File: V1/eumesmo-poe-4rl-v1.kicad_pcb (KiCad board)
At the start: 4 copper layers, 99.5 x 45 mm, 125 parts, among them J1 USB_C_Receptacle_USB2.0, J2 RJ45 JACK, J3 250-202, J4 250-202, J5 250-202, J6 250-202, K1 G5NB-1A-E-DC5, K2 G5NB-1A-E-DC5, K3 G5NB-1A-E-DC5, K4 G5NB-1A-E-DC5, Q1 UMH3N, Q2 WPM2015-3/TR, Q3 LMUN2211LT1G, Q4 MMBT2222A, Q5 MMBT2222A, Q6 MMBT2222A, Q7 MMBT2222A, SW1 RESET, U1 CH340K, U2 ESP32-WROOM-32UE-N16, U3 LAN8710A, U4 TPS2376DDAR-H, U5 TX4138, U6 SY8089A1AAC

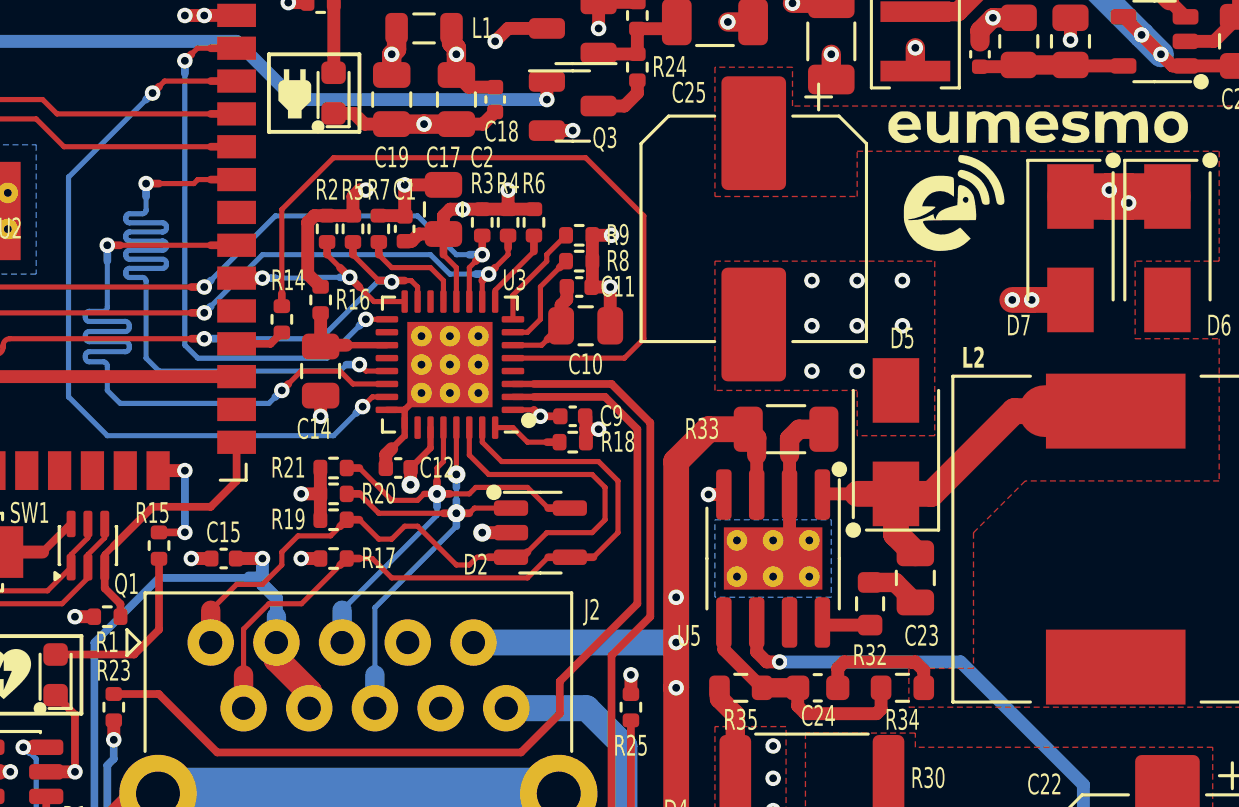
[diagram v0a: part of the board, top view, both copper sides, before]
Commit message: Tweaks to the ethernet signals tracks.
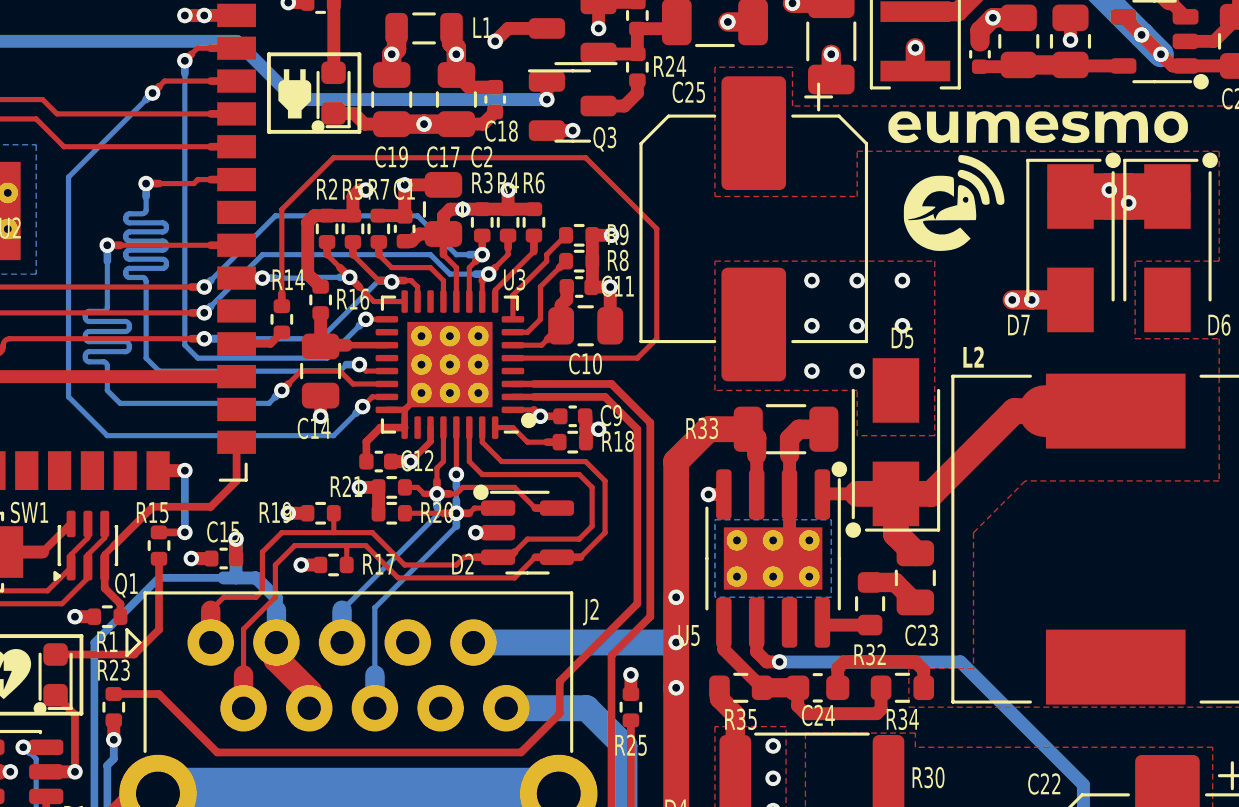
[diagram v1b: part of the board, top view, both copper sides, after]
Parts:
- moved R20 2.37 mm to (140.5, 93.2)
- moved R21 2.37 mm to (140.5, 92.2)
- moved C12 0.79 mm to (140.0, 91.2)
- moved R19 0.56 mm to (137.8, 93.2)
- moved D2 0.50 mm to (145.8, 94.0)
- moved R17 0.25 mm to (138.2, 95.2)
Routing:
- net /ETHTXD-: track 19.6 -> 16.4 mm
- net /ETHTXD+: track 18.9 -> 15.8 mm
- net +3V3A: track 47.2 -> 46.3 mm, vias 6 -> 7
- net /ETHRXD+: track 28.1 -> 29.0 mm
- net /EMACCLK: track 29.6 -> 30.3 mm
- net GND: track 74.2 -> 74.9 mm

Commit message: LEDs replaced for orange
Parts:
- D11, D12, D15, D16, D3, D8: value WHITE/0603 -> ORANGE/0603
- R15, R37: value 330R -> 680R
- R39, R40, R45, R46: value 1k -> 1.2k
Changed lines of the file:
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@@
 			)
 		)
-		(property "Value" "1k"
+		(property "Value" "1.2k"
 			(at 0 1.17 0)
 			(layer "F.Fab")
@@
 			)
 		)
-		(property "Mfr PN" "0402WGF1001TCE"
+		(property "Mfr PN" "0402WGF1201TCE"
 			(at 0 0 180)
 			(unlocked yes)
@@
 			)
 		)
-		(property "Vendor PN" "C11702"
+		(property "Vendor PN" "C25862"
 			(at 0 0 180)
 			(unlocked yes)
@@
 			)
 		)
-		(property "LCSC Part #" "C11702"
+		(property "LCSC Part #" "C25862"
 			(at 0 0 180)
 			(unlocked yes)
@@
 			)
 		)
-		(property "Value" "1k"
+		(property "Value" "1.2k"
 			(at 0 1.17 0)
 			(layer "F.Fab")
@@
 			)
 		)
-		(property "Mfr PN" "0402WGF1001TCE"
+		(property "Mfr PN" "0402WGF1201TCE"
 			(at 0 0 180)
 			(unlocked yes)
@@
 			)
 		)
-		(property "Vendor PN" "C11702"
+		(property "Vendor PN" "C25862"
 			(at 0 0 180)
 			(unlocked yes)
@@
 			)
 		)
-		(property "LCSC Part #" "C11702"
+		(property "LCSC Part #" "C25862"
 			(at 0 0 180)
 			(unlocked yes)
@@
 			)
 		)
-		(property "Value" "WHITE/0603"
+		(property "Value" "ORANGE/0603"
 			(at 0 1.43 0)
 			(layer "F.Fab")
@@
 			)
 		)
-		(property "Mfr" "Hubei KENTO Elec"
+		(property "Mfr" "Everlight Elec"
 			(at 0 0 0)
 			(unlocked yes)
@@
 			)
 		)
-		(property "Mfr PN" "KT-0603W"
+		(property "Mfr PN" "19-217/S2C-AL1M2VY/6T"
 			(at 0 0 0)
 			(unlocked yes)
@@
 			)
 		)
-		(property "Technology" "InGaN"
+		(property "Technology" "LED"
 			(at 0 0 0)
 			(unlocked yes)
@@
 			)
 		)
-		(property "Vendor PN" "C2290"
+		(property "Vendor PN" "C2987557"
 			(at 0 0 0)
 			(unlocked yes)
@@
 			)
 		)
-		(property "LCSC Part #" "C2290"
+		(property "LCSC Part #" "C2987557"
 			(at 0 0 0)
 			(unlocked yes)
@@
 			(unit
 				(name "A")
-				(pins "3" "4" "5" "21" "22" "17" "18" "20" "19" "32" "2" "1" "38" "39"
-					"15" "25" "35" "24" "34" "26" "29" "14" "16" "13" "23" "27" "28" "30"
+				(pins "3" "4" "5" "21" "22" "17" "18" "20" "19" "32" "2" "1" "38" "15"
+					"39" "25" "35" "24" "34" "26" "29" "14" "16" "13" "23" "27" "28" "30"
 					"31" "33" "36" "37" "10" "11" "12" "8" "9" "6" "7"
 				)
@@
 			)
 		)
-		(property "Value" "WHITE/0603"
+		(property "Value" "ORANGE/0603"
 			(at 0 1.43 0)
 			(layer "F.Fab")
@@
 			)
 		)
-		(property "Mfr" "Hubei KENTO Elec"
+		(property "Mfr" "Everlight Elec"
 			(at 0 0 0)
 			(unlocked yes)
@@
 			)
 		)
-		(property "Mfr PN" "KT-0603W"
+		(property "Mfr PN" "19-217/S2C-AL1M2VY/6T"
 			(at 0 0 0)
 			(unlocked yes)
@@
 			)
 		)
-		(property "Technology" "InGaN"
+		(property "Technology" "LED"
 			(at 0 0 0)
 			(unlocked yes)
@@
 			)
 		)
-		(property "Vendor PN" "C2290"
+		(property "Vendor PN" "C2987557"
 			(at 0 0 0)
 			(unlocked yes)
@@
 			)
 		)
-		(property "LCSC Part #" "C2290"
+		(property "LCSC Part #" "C2987557"
 			(at 0 0 0)
 			(unlocked yes)
@@
 			)
 		)
-		(property "Value" "1k"
+		(property "Value" "1.2k"
 			(at 0 1.17 0)
 			(layer "F.Fab")
@@
 			)
 		)
-		(property "Mfr PN" "0402WGF1001TCE"
+		(property "Mfr PN" "0402WGF1201TCE"
 			(at 0 0 180)
 			(unlocked yes)
@@
 			)
 		)
-		(property "Vendor PN" "C11702"
+		(property "Vendor PN" "C25862"
 			(at 0 0 180)
 			(unlocked yes)
@@
 			)
 		)
-		(property "LCSC Part #" "C11702"
+		(property "LCSC Part #" "C25862"
 			(at 0 0 180)
 			(unlocked yes)
@@
 			)
 		)
-		(property "Value" "1k"
+		(property "Value" "1.2k"
 			(at 0 1.17 0)
 			(layer "F.Fab")
@@
 			)
 		)
-		(property "Mfr PN" "0402WGF1001TCE"
+		(property "Mfr PN" "0402WGF1201TCE"
 			(at 0 0 180)
 			(unlocked yes)
@@
 			)
 		)
-		(property "Vendor PN" "C11702"
+		(property "Vendor PN" "C25862"
 			(at 0 0 180)
 			(unlocked yes)
@@
 			)
 		)
-		(property "LCSC Part #" "C11702"
+		(property "LCSC Part #" "C25862"
 			(at 0 0 180)
 			(unlocked yes)
@@
 			)
 		)
-		(property "Value" "330R"
+		(property "Value" "680R"
 			(at 0 1.17 90)
 			(layer "F.Fab")
@@
 			)
 		)
-		(property "Mfr PN" "0402WGF3300TCE"
+		(property "Mfr PN" "0402WGF6800TCE"
 			(at 0 0 270)
 			(unlocked yes)
@@
 			)
 		)
-		(property "Vendor PN" "C25104"
+		(property "Vendor PN" "C25130"
 			(at 0 0 270)
 			(unlocked yes)
@@
 			)
 		)
-		(property "LCSC Part #" "C25104"
+		(property "LCSC Part #" "C25130"
 			(at 0 0 270)
 			(unlocked yes)
@@
 			)
 		)
-		(property "Value" "WHITE/0603"
+		(property "Value" "ORANGE/0603"
 			(at 0 1.43 90)
 			(layer "F.Fab")
@@
 			)
 		)
-		(property "Mfr" "Hubei KENTO Elec"
+		(property "Mfr" "Everlight Elec"
 			(at 0 0 90)
 			(unlocked yes)
@@
 			)
 		)
-		(property "Mfr PN" "KT-0603W"
+		(property "Mfr PN" "19-217/S2C-AL1M2VY/6T"
 			(at 0 0 90)
 			(unlocked yes)
@@
 			)
 		)
-		(property "Vendor PN" "C2290"
+		(property "Vendor PN" "C2987557"
 			(at 0 0 90)
 			(unlocked yes)
@@
 			)
 		)
-		(property "LCSC Part #" "C2290"
+		(property "LCSC Part #" "C2987557"
 			(at 0 0 90)
 			(unlocked yes)
@@
 			)
 		)
+		(property "Package" "0603/1608"
+			(at 0 0 90)
+			(unlocked yes)
+			(layer "F.Fab")
+			(hide yes)
+			(effects
+				(font
+					(size 1 1)
+					(thickness 0.15)
+				)
+			)
+		)
 		(property ki_fp_filters "LED* LED_SMD:* LED_THT:*")
 		(sheetname "/")
@@
 			)
 		)
-		(property "Value" "WHITE/0603"
+		(property "Value" "ORANGE/0603"
 			(at 0 1.43 0)
 			(layer "F.Fab")
@@
 			)
 		)
-		(property "Mfr" "Hubei KENTO Elec"
+		(property "Mfr" "Everlight Elec"
 			(at 0 0 0)
 			(unlocked yes)
@@
 			)
 		)
-		(property "Mfr PN" "KT-0603W"
+		(property "Mfr PN" "19-217/S2C-AL1M2VY/6T"
 			(at 0 0 0)
 			(unlocked yes)
@@
 			)
 		)
-		(property "Technology" "InGaN"
+		(property "Technology" "LED"
 			(at 0 0 0)
 			(unlocked yes)
@@
 			)
 		)
-		(property "Vendor PN" "C2290"
+		(property "Vendor PN" "C2987557"
 			(at 0 0 0)
 			(unlocked yes)
@@
 			)
 		)
-		(property "LCSC Part #" "C2290"
+		(property "LCSC Part #" "C2987557"
 			(at 0 0 0)
 			(unlocked yes)
@@
 			)
 		)
-		(property "Value" "WHITE/0603"
+		(property "Value" "ORANGE/0603"
 			(at 0 1.43 0)
 			(layer "F.Fab")
@@
 			)
 		)
-		(property "Mfr" "Hubei KENTO Elec"
+		(property "Mfr" "Everlight Elec"
 			(at 0 0 0)
 			(unlocked yes)
@@
 			)
 		)
-		(property "Mfr PN" "KT-0603W"
+		(property "Mfr PN" "19-217/S2C-AL1M2VY/6T"
 			(at 0 0 0)
 			(unlocked yes)
@@
 			)
 		)
-		(property "Technology" "InGaN"
+		(property "Technology" "LED"
 			(at 0 0 0)
 			(unlocked yes)
@@
 			)
 		)
-		(property "Vendor PN" "C2290"
+		(property "Vendor PN" "C2987557"
 			(at 0 0 0)
 			(unlocked yes)
@@
 			)
 		)
-		(property "LCSC Part #" "C2290"
+		(property "LCSC Part #" "C2987557"
 			(at 0 0 0)
 			(unlocked yes)
@@
 			)
 		)
-		(property "Value" "WHITE/0603"
+		(property "Value" "ORANGE/0603"
 			(at 0 1.43 90)
 			(layer "F.Fab")
@@
 			)
 		)
-		(property "Mfr" "Hubei KENTO Elec"
+		(property "Mfr" "Everlight Elec"
 			(at 0 0 90)
 			(unlocked yes)
@@
 			)
 		)
-		(property "Mfr PN" "KT-0603W"
+		(property "Mfr PN" "19-217/S2C-AL1M2VY/6T"
 			(at 0 0 90)
 			(unlocked yes)
@@
 			)
 		)
-		(property "Technology" "InGaN"
+		(property "Technology" "LED"
 			(at 0 0 90)
 			(unlocked yes)
@@
 			)
 		)
-		(property "Vendor PN" "C2290"
+		(property "Vendor PN" "C2987557"
 			(at 0 0 90)
 			(unlocked yes)
@@
 			)
 		)
-		(property "LCSC Part #" "C2290"
+		(property "LCSC Part #" "C2987557"
 			(at 0 0 90)
 			(unlocked yes)
@@
 			)
 		)
-		(property "Value" "330R"
+		(property "Value" "680R"
 			(at 0 1.17 0)
 			(layer "F.Fab")
@@
 			)
 		)
-		(property "Mfr PN" "0402WGF3300TCE"
+		(property "Mfr PN" "0402WGF6800TCE"
 			(at 0 0 0)
 			(unlocked yes)
@@
 			)
 		)
-		(property "Vendor PN" "C25104"
+		(property "Vendor PN" "C25130"
 			(at 0 0 0)
 			(unlocked yes)
@@
 			)
 		)
-		(property "LCSC Part #" "C25104"
+		(property "LCSC Part #" "C25130"
 			(at 0 0 0)
 			(unlocked yes)
